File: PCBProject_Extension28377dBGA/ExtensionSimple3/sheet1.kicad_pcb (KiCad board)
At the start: 4 copper layers, 140.3 x 101.7 mm, 121 parts, among them J1 Conn_02x05_Odd_Even, J2 Conn_01x02_Pin, J3 Conn_01x02_Pin, J4 Conn_01x02_Pin, J5 Conn_01x02_Pin, J6 Conn_02x05_Odd_Even, Q1 FMMT618TA, U1 SN74ABT541, U2 SN74ABT541

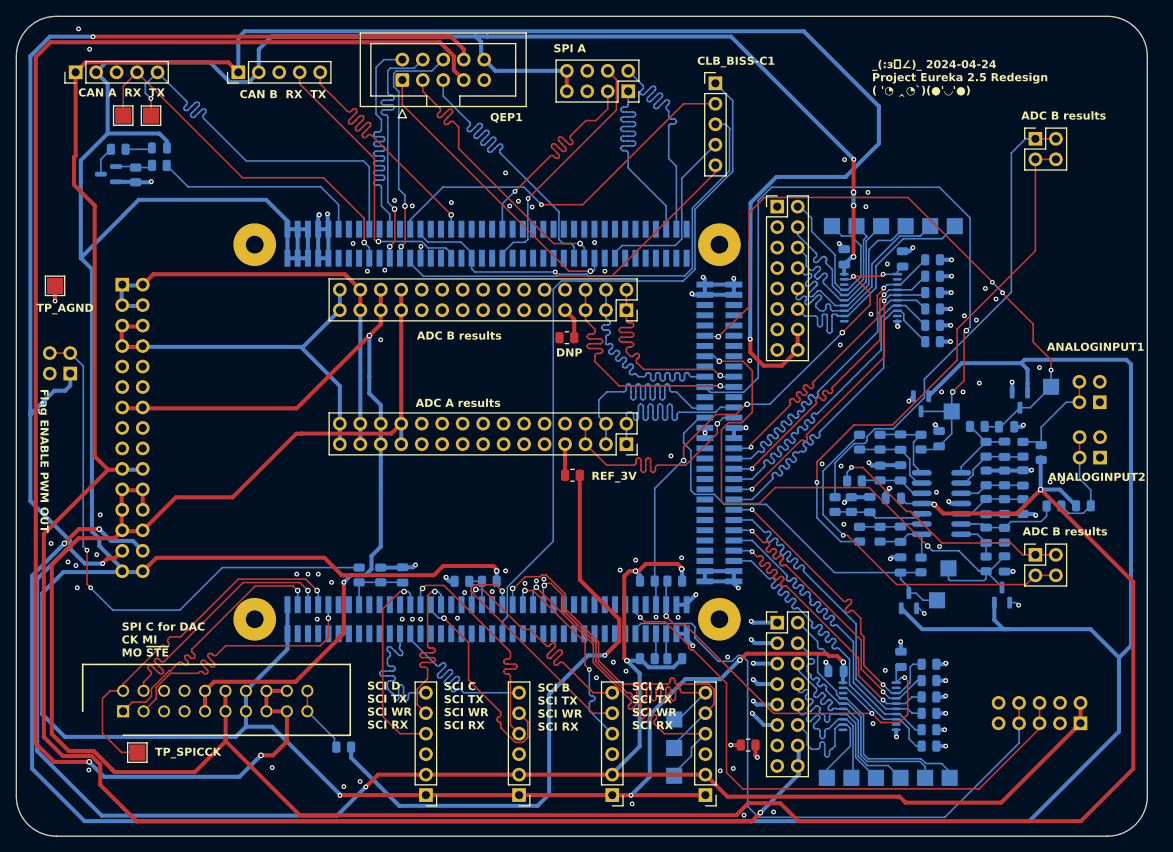
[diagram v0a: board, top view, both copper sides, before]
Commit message: Divide DSP, and Matched DC bus Net Lengths
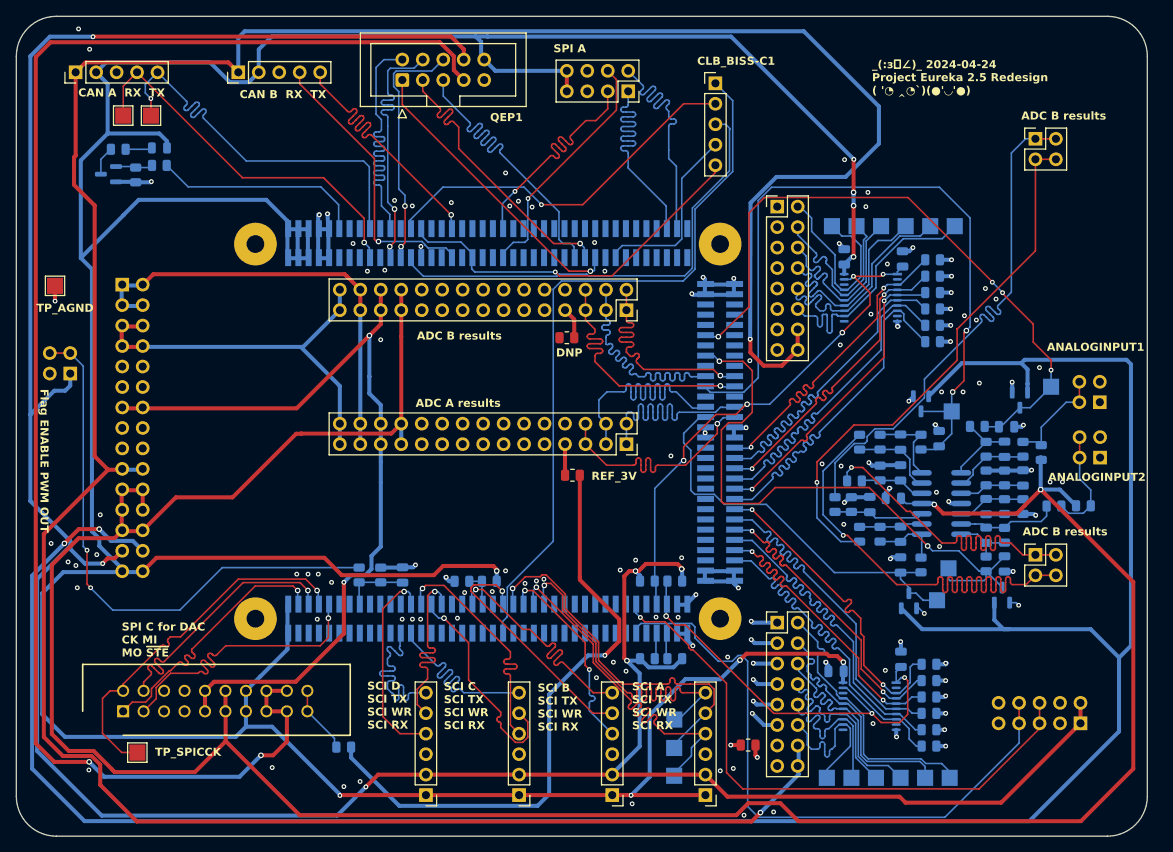
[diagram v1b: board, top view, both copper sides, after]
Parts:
- added DSP2: TMS320F28377D-BGA-P1B, 1mmlab_footprint:DSP_240_P1B, B.Cu at (285.8, 95.1)
- added DSP3: TMS320F28377D-BGA-P1C, 1mmlab_footprint:DSP_240_P1C, B.Cu at (285.8, 95.1)
- DSP1: value ~ -> TMS320F28377D-BGA-P1A; footprint 1mmlab_footprint:DSP_240_SMD -> 1mmlab_footprint:DSP_240_P1A
- moved DSP1 0.11 mm to (285.8, 95.1)
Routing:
- net /GND_2M2: track 44.8 -> 69.5 mm
- net /DC_BUS_2M2: track 32.0 -> 45.5 mm
- net /DC_BUS_2M1: track 60.3 -> 65.6 mm

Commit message: fix SCI_C AND D, ADD ECAP TO 1TO2
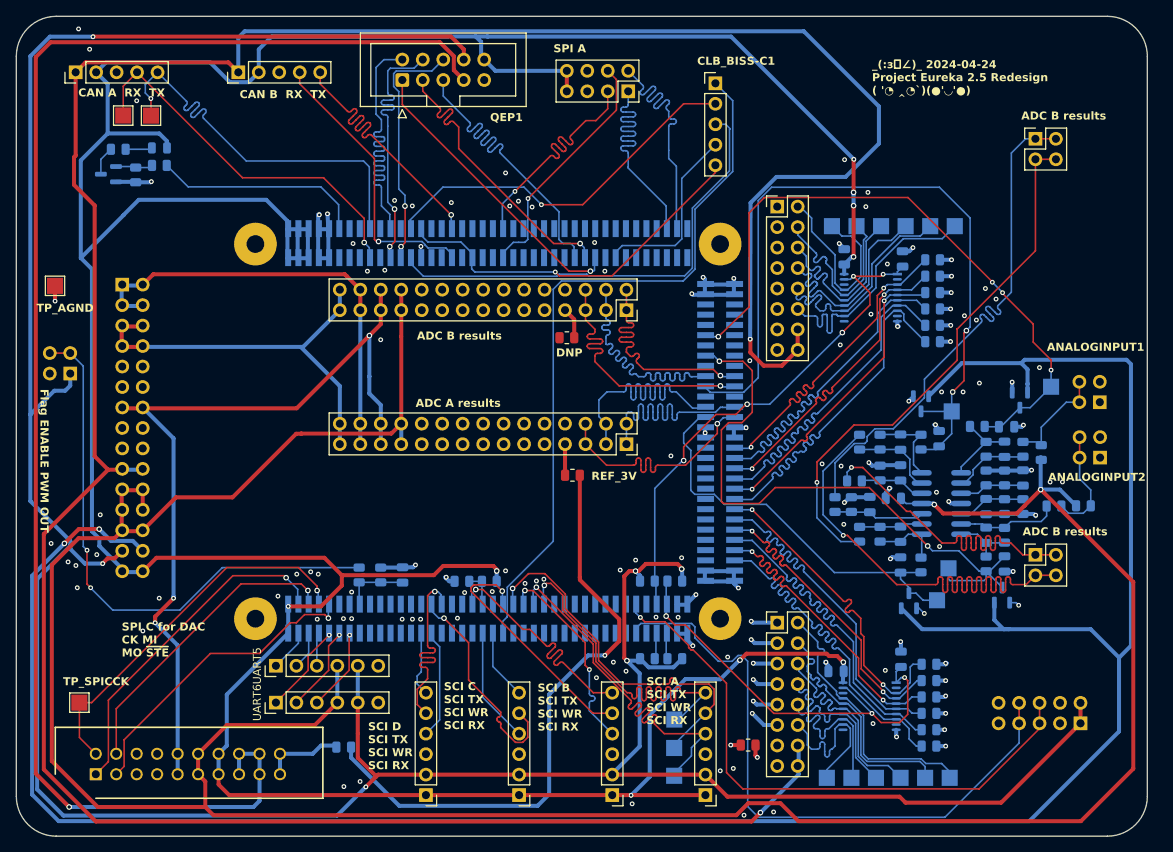
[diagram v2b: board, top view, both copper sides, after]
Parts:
- added UART5: Conn_01x06, Connector_PinHeader_2.54mm:PinHeader_1x06_P2.54mm_Vertical, F.Cu at (216.8, 142.3)
- added UART6: Conn_01x06, Connector_PinHeader_2.54mm:PinHeader_1x06_P2.54mm_Vertical, F.Cu at (216.8, 146.9)
- moved TESTPOINT4 9.49 mm to (192.4, 146.9)
- moved SPI-DAC2 8.52 mm to (194.4, 155.8)
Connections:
- DSP2 pad 104: /UART_SCI_TXDD -> unconnected-(DSP2-A9_104-Pad104)
- DSP2 pad 105: /UART_SCI_RXDD -> unconnected-(DSP2-105_D4-Pad105)
- DSP2 pad 106: /UART_SCI_TXDC -> unconnected-(DSP2-A8_106-Pad106)
- DSP2 pad 107: /UART_SCI_RXDC -> unconnected-(DSP2-107_D3-Pad107)
- DSP2 pad 108: unconnected-(DSP2-A7_108-Pad108) -> /UART_SCI_TXDD
- DSP2 pad 110: unconnected-(DSP2-A6_110-Pad110) -> /UART_SCI_RXDD
- DSP2 pad 120: unconnected-(DSP2-A1_120-Pad120) -> /UART_SCI_RXDC
- DSP2 pad 122: unconnected-(DSP2-A0_122-Pad122) -> /UART_SCI_TXDC
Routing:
- net D+5V: track 481.6 -> 446.2 mm
- net A+5V: track 321.0 -> 344.9 mm
- net VDD: track 352.3 -> 369.7 mm
- net /UART_SCI_TXDC: track 25.9 -> 8.74 mm
- net /UART_SCI_RXDC: track 31.2 -> 14.3 mm, vias 1 -> 0
- net /UART_SCI_TXDD: track 24.7 -> 8.05 mm
- net /UART_SCI_RXDD: track 25.5 -> 13.6 mm, vias 1 -> 0
- net /ECAP4_IPM_TerminalDutyU2: track 0.00 -> 11.1 mm, vias 0 -> 1
- net /ECAP5_IPM_TerminalDutyV2: track 0.00 -> 10.6 mm, vias 0 -> 1
- net /ECAP6_IPM_TerminalDutyW2: track 0.00 -> 10.1 mm, vias 0 -> 1
- net /SPI_C_MO_HS: track 33.4 -> 43.0 mm
- net /ECAP1_IPM_TerminalDutyU1: track 0.00 -> 5.20 mm
- net /ECAP2_IPM_TerminalDutyV1: track 0.00 -> 4.68 mm
- net /SPI_C_MI_HS: track 33.4 -> 37.9 mm
- net /ECAP3_IPM_TerminalDutyW1: track 0.00 -> 4.15 mm
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
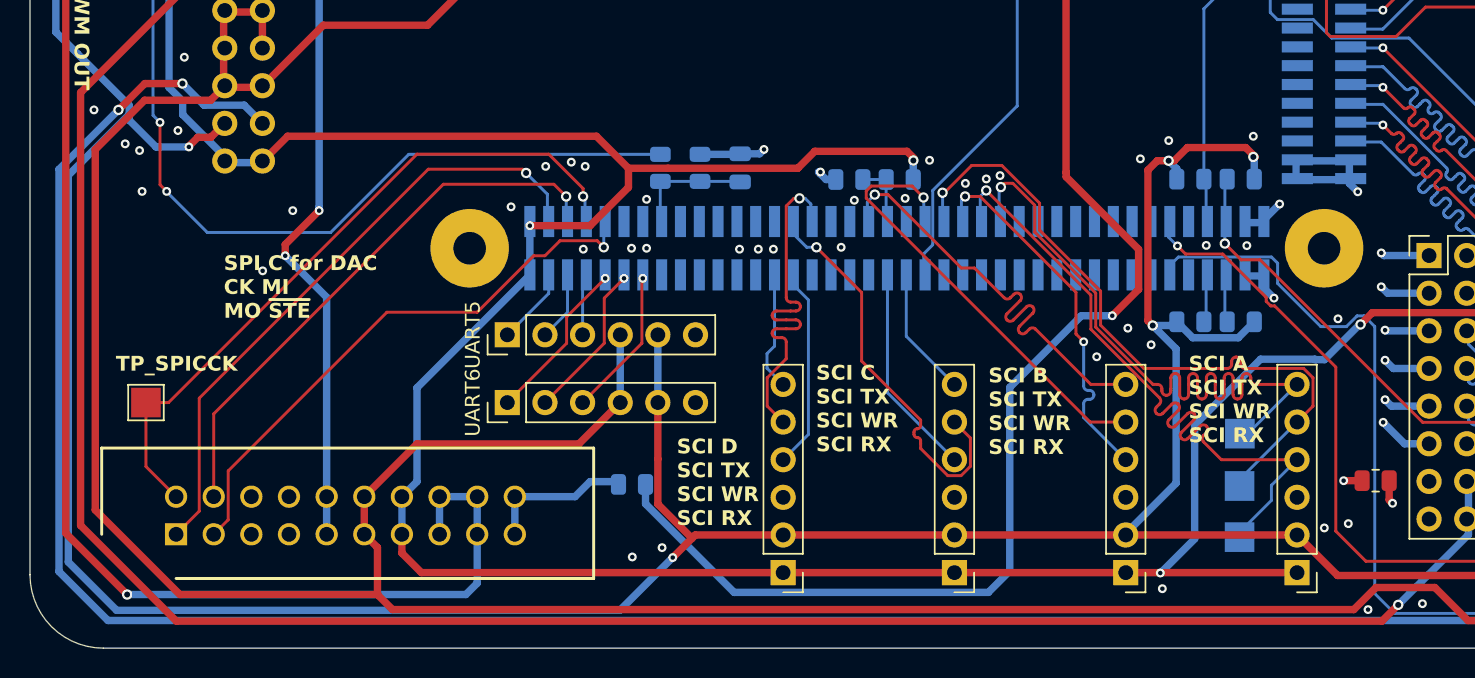
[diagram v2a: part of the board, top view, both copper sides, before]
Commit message: fix SCI_C and D, add ECAP to 1TO4, but 1TO4 haven't finish.
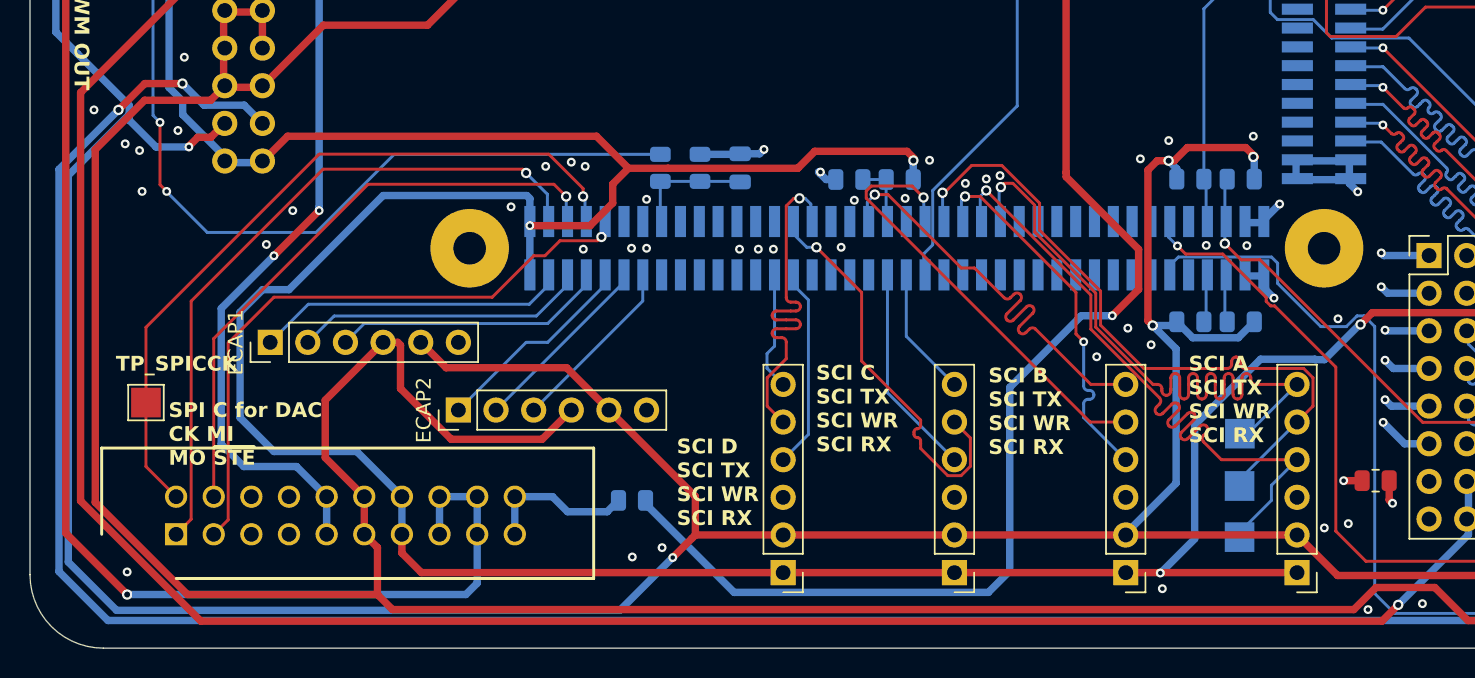
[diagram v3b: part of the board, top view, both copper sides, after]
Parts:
- removed UART5, UART6: Conn_01x06, Connector_PinHeader_2.54mm:PinHeader_1x06_P2.54mm_Vertical
- added ECAP1: Conn_01x06, Connector_PinHeader_2.54mm:PinHeader_1x06_P2.54mm_Vertical, F.Cu at (200.8, 142.8)
- added ECAP2: Conn_01x06, Connector_PinHeader_2.54mm:PinHeader_1x06_P2.54mm_Vertical, F.Cu at (213.5, 147.4)
- moved RU5 1.08 mm to (225.2, 153.5)
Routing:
- net D+5V: track 446.2 -> 472.4 mm
- net /ECAP1_IPM_TerminalDutyU1: track 5.20 -> 21.1 mm
- net /ECAP2_IPM_TerminalDutyV1: track 4.68 -> 19.8 mm
- net /ECAP3_IPM_TerminalDutyW1: track 4.15 -> 18.5 mm
- net VDD: track 369.7 -> 380.5 mm
- net A+5V: track 344.9 -> 351.2 mm
- net A-5V: track 104.3 -> 109.9 mm
- net /~{SPI_C_STE_HS}: track 38.3 -> 42.5 mm
- net /SPI_C_MO_HS: track 43.0 -> 47.1 mm
- net /SPI_C_MI_HS: track 37.9 -> 40.9 mm
- net /SPI_C_CK_HS: track 46.9 -> 49.9 mm
- net /ECAP4_IPM_TerminalDutyU2: track 11.1 -> 14.1 mm, vias 1 -> 0
- net /ECAP6_IPM_TerminalDutyW2: track 10.1 -> 12.2 mm, vias 1 -> 0
- net /ECAP5_IPM_TerminalDutyV2: track 10.6 -> 12.7 mm, vias 1 -> 0
- net REF_3V: track 75.4 -> 74.4 mm
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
